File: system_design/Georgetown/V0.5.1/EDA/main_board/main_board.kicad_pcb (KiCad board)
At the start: 2 copper layers, 40.6 x 82.6 mm, 34 parts, among them J1 B3B-XH-A_LF__SN_, J2 Conn_01x02_Pin, P1 SD card socket, SW1 SW_Wuerth_450301014042, U1 HX-2S-JH10, U2 DS3231M, U3 INA219AxD, U4 BME280_module, U5 KA78M05_TO252

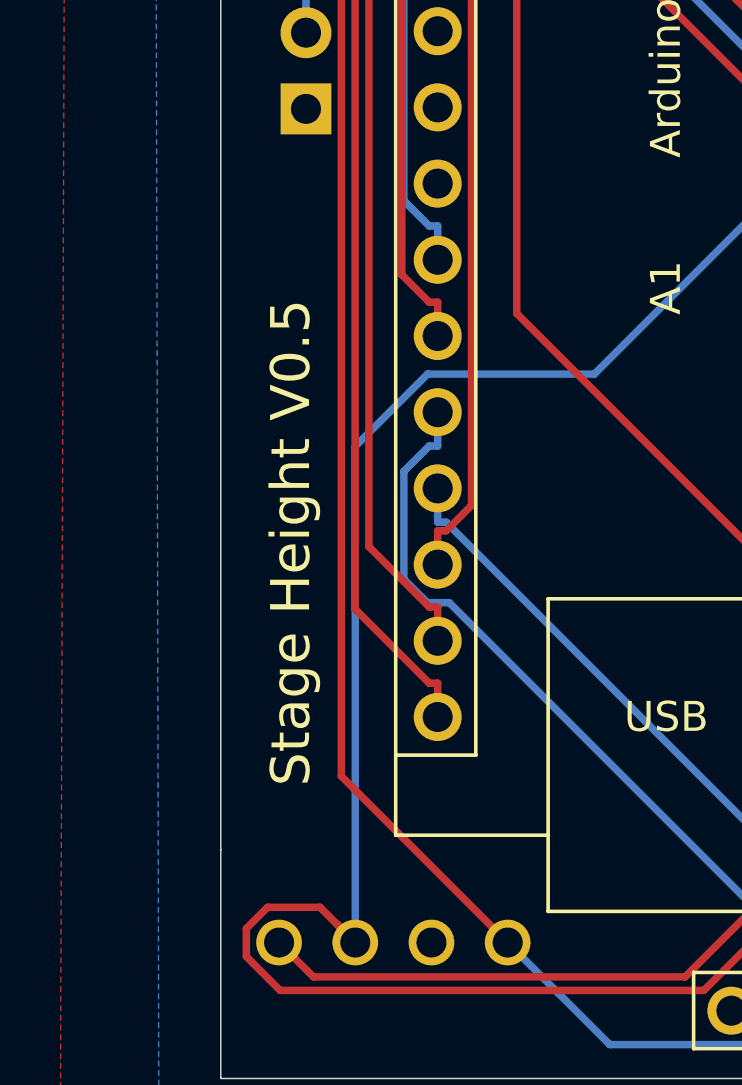
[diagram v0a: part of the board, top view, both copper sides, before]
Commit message: SilkScreenUpdated
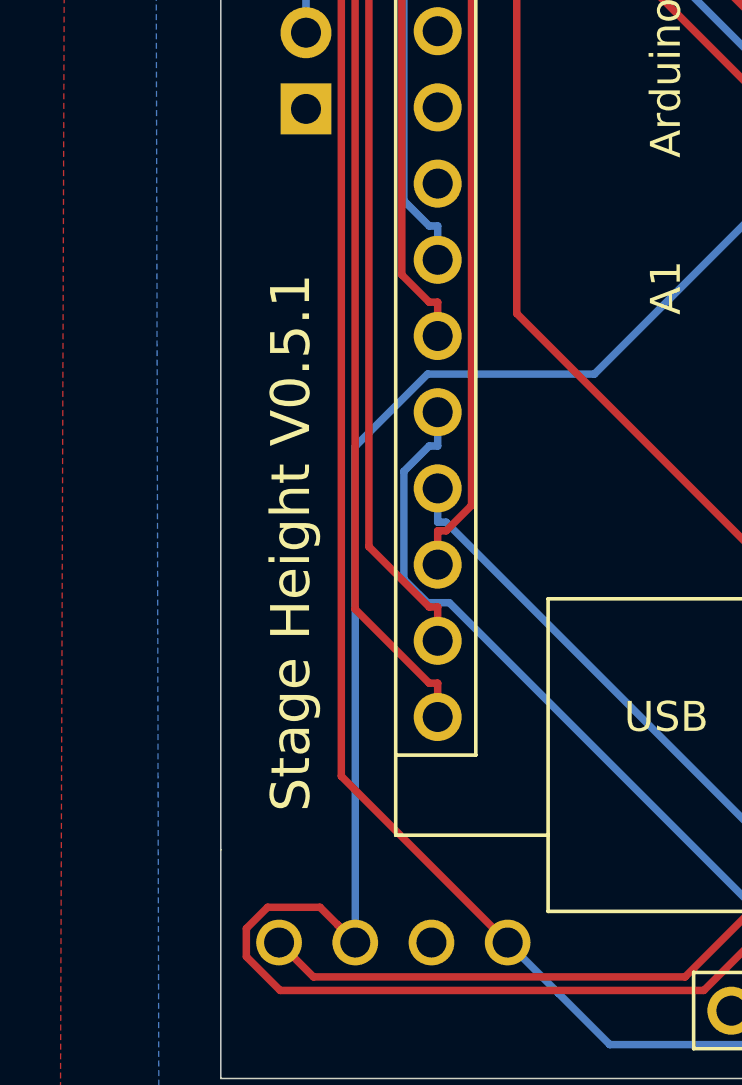
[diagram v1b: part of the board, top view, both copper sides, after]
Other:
- board text added: "Stage Height V0.5.1"
- board text removed: "Stage Height V0.5"
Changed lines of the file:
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@@
 		)
 	)
-	(gr_text "Stage Height V0.5"
+	(gr_text "Stage Height V0.5.1"
 		(at 139.5 132 90)
 		(layer "F.SilkS")
